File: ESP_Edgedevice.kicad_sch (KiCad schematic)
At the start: 0 parts

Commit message: Schematic Of Relay Portion Completed
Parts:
- added J1: Screw_Terminal_01x03, symbol Connector:Screw_Terminal_01x03
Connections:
- new net COM: J1.2 (Pin_2)
- new net NC: J1.3 (Pin_3)
- new net NO: J1.1 (Pin_1)
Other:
- added sheet Relay (relay.kicad_sch)
- title: (none) -> ${project_name}

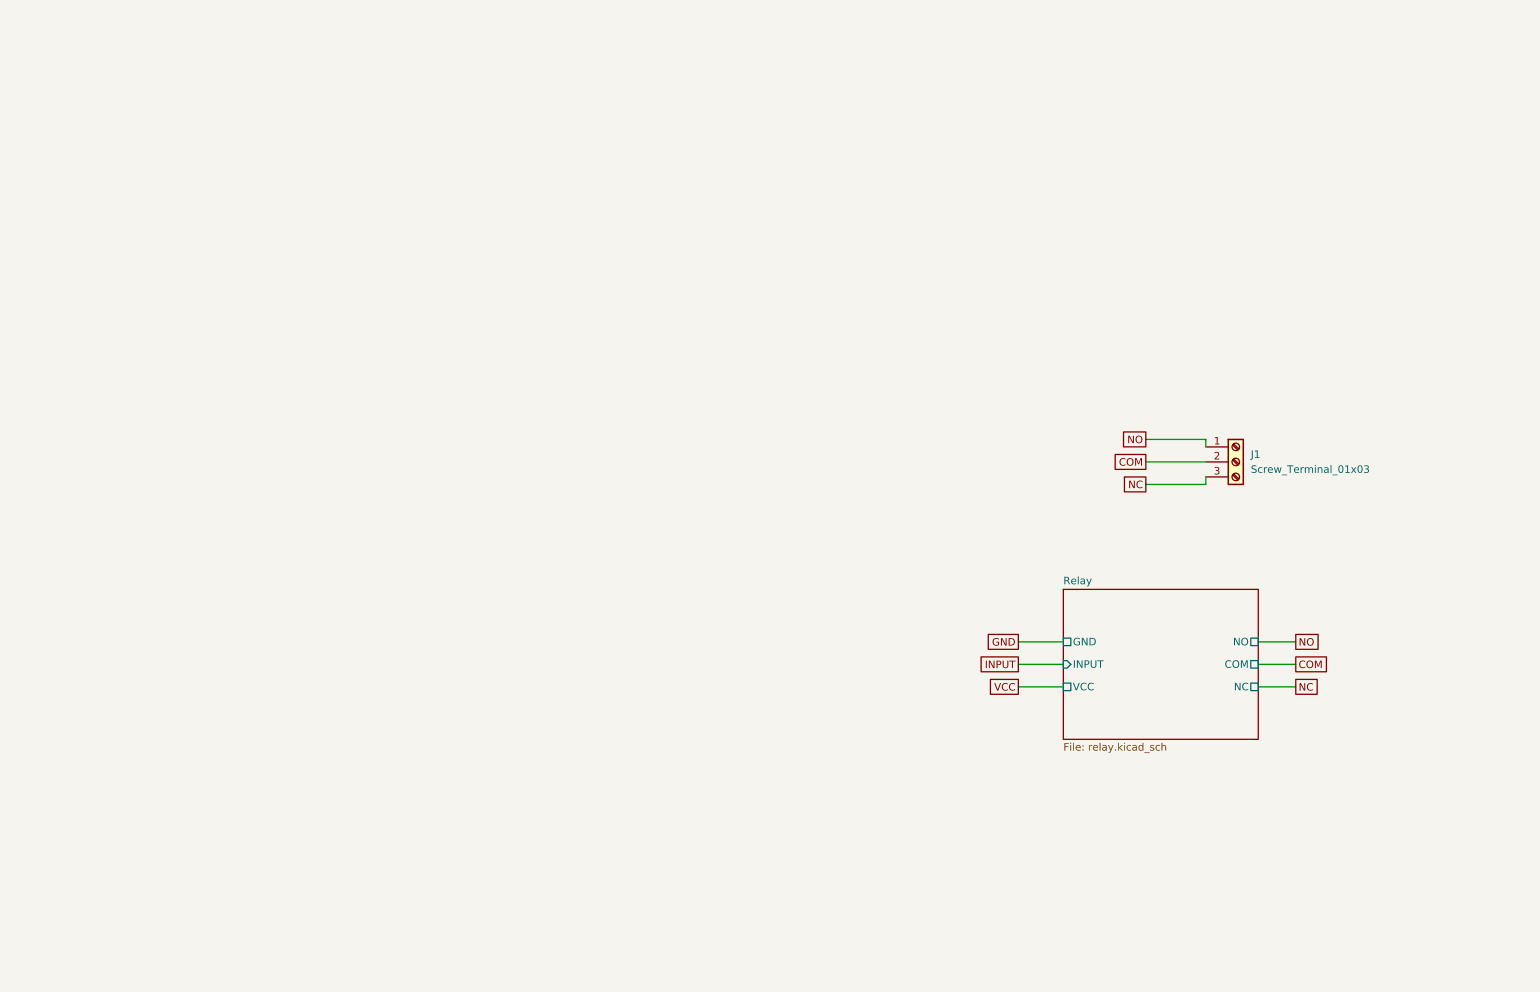
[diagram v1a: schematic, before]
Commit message: Amc1200 Based Voltage Sensing Schematic Completed
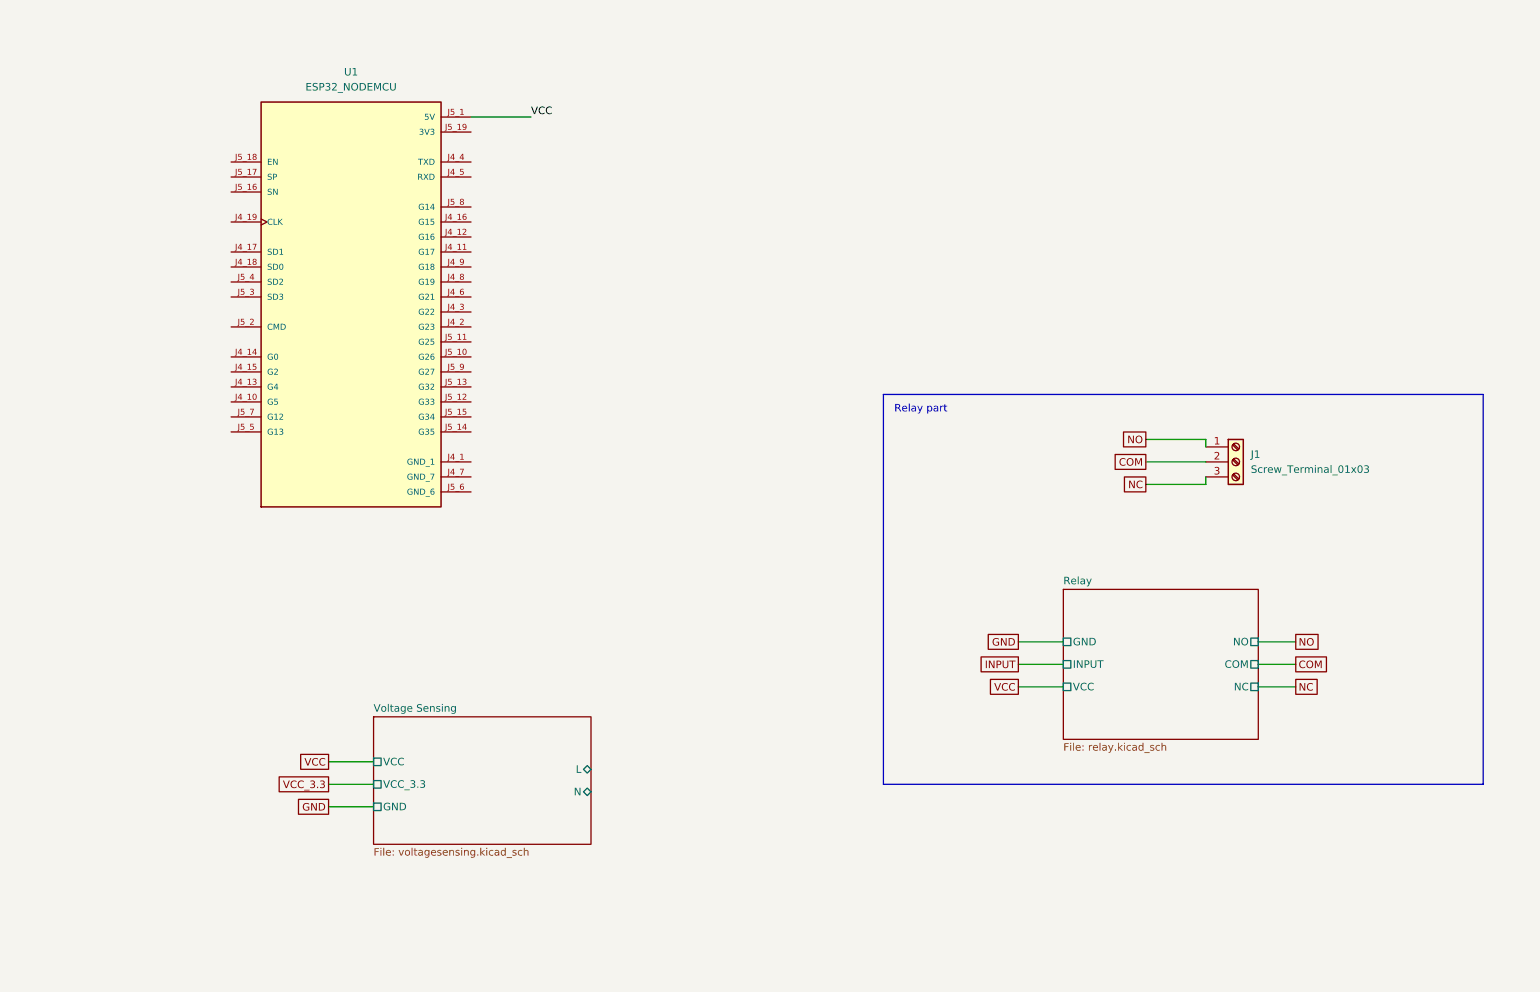
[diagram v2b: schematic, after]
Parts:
- added U1: ESP32_NODEMCU, ESP32_NODEMCU:MODULE_ESP32_NODEMCU, symbol ESP32_NODEMCU:ESP32_NODEMCU
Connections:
- net VCC: now also U1.J5_1 (5V)
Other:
- added sheet Voltage Sensing (voltagesensing.kicad_sch)
- note added: "Relay part"

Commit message: minor changes
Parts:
- added H1, H2, H3, H4: MountingHole, symbol Mechanical:MountingHole
- added PS1: HLK-5M05, HLK-5M05:CONV_HLK-5M05, symbol HLK-5M05:HLK-5M05
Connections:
- net GND: now also U1.J4_1 (GND_1), PS1.3 (-VO)
- net VCC: now also PS1.4 (+VO)
- net VCC_3.3: now also U1.J5_19 (3V3)
- new net LIVE: PS1.1 (AC1)
- new net NEUTRAL: PS1.2 (AC2)
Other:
- moved on the sheet: J1, U1

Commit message: Final Schematic Editing Completed
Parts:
- removed PS1: HLK-5M05, HLK-5M05:CONV_HLK-5M05, symbol HLK-5M05:HLK-5M05
- added H1: WIZ850IO, WIZ850IO:WIZ850IO, symbol WIZ850IO:WIZ850IO
- added J1, J4: Conn_01x04_Socket, symbol Connector:Conn_01x04_Socket
- added J3: Screw_Terminal_01x02, symbol Connector:Screw_Terminal_01x02
- added PS1: HLK-5M05, Converter_ACDC:Converter_ACDC_Hi-Link_HLK-5Mxx, symbol Converter_ACDC:HLK-5M05
- added R1, R2: 10K, symbol Device:R
- renumbered H1 to H2, H2 to H3, H3 to H4, H4 to H5, J1 to J2
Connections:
- net GND: now also U1.J4_7 (GND_7), U1.J5_6 (GND_6), H1.1 (GND_1), H1.2 (GND_2), H1.7 (GND_3), J1.4 (Pin_4), PS1.3 (-Vout)
- net INPUT: now also U1.J5_11 (G25)
- net LIVE: now also J3.1 (Pin_1), J4.1 (Pin_1), PS1.1 (AC/L)
- net NEUTRAL: now also J3.2 (Pin_2), J4.2 (Pin_2), PS1.2 (AC/N)
- net VCC: now also J1.1 (Pin_1), PS1.4 (+Vout)
- net VCC_3.3: now also H1.8 (3.3V_1), H1.9 (3.3V_2), R1.1, R2.1
- net CS: now reaches U1.J4_10 (G5)
- net CS: now also H1.5 (SCNN)
- net RX: now reaches U1.J4_11 (G17)
- net RX: now also J1.2 (Pin_2)
- net TX: now reaches U1.J4_12 (G16)
- net TX: now also J1.3 (Pin_3)
- net RESET: now reaches U1.J4_13 (G4)
- net RESET: now also H1.11 (RSTN), R2.2
- net MOSI: now reaches U1.J4_2 (G23)
- net MOSI: now also H1.3 (MOSI)
- net MISO: now reaches U1.J4_8 (G19)
- net MISO: now also H1.12 (MISO)
- net SCK: now reaches U1.J4_9 (G18)
- net SCK: now also H1.4 (SCLK)
- net AC sensing: now reaches U1.J5_15 (G34)
- net INT: now reaches U1.J5_7 (G12)
- net INT: now also H1.6 (INTN), R1.2
- new net CTa: J4.3 (Pin_3)
- new net CTb: J4.4 (Pin_4)
- no-connect marks 0 -> 23
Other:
- sheet Relay ports: added none; removed GND
- sheet Voltage Sensing ports: added none; removed GND, VCC
- note added: "AMC1200 based voltage sensing"
- note added: "Ethernet"
- note added: "Hilink 5v/5W powersupply"
- moved on the sheet: J2
